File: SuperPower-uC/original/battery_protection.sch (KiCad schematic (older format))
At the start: 11 parts, among them J1 JST_PH_S2B_thru, Q1 DMN2019UTS, U1 AP9101CK6-AYTRG1

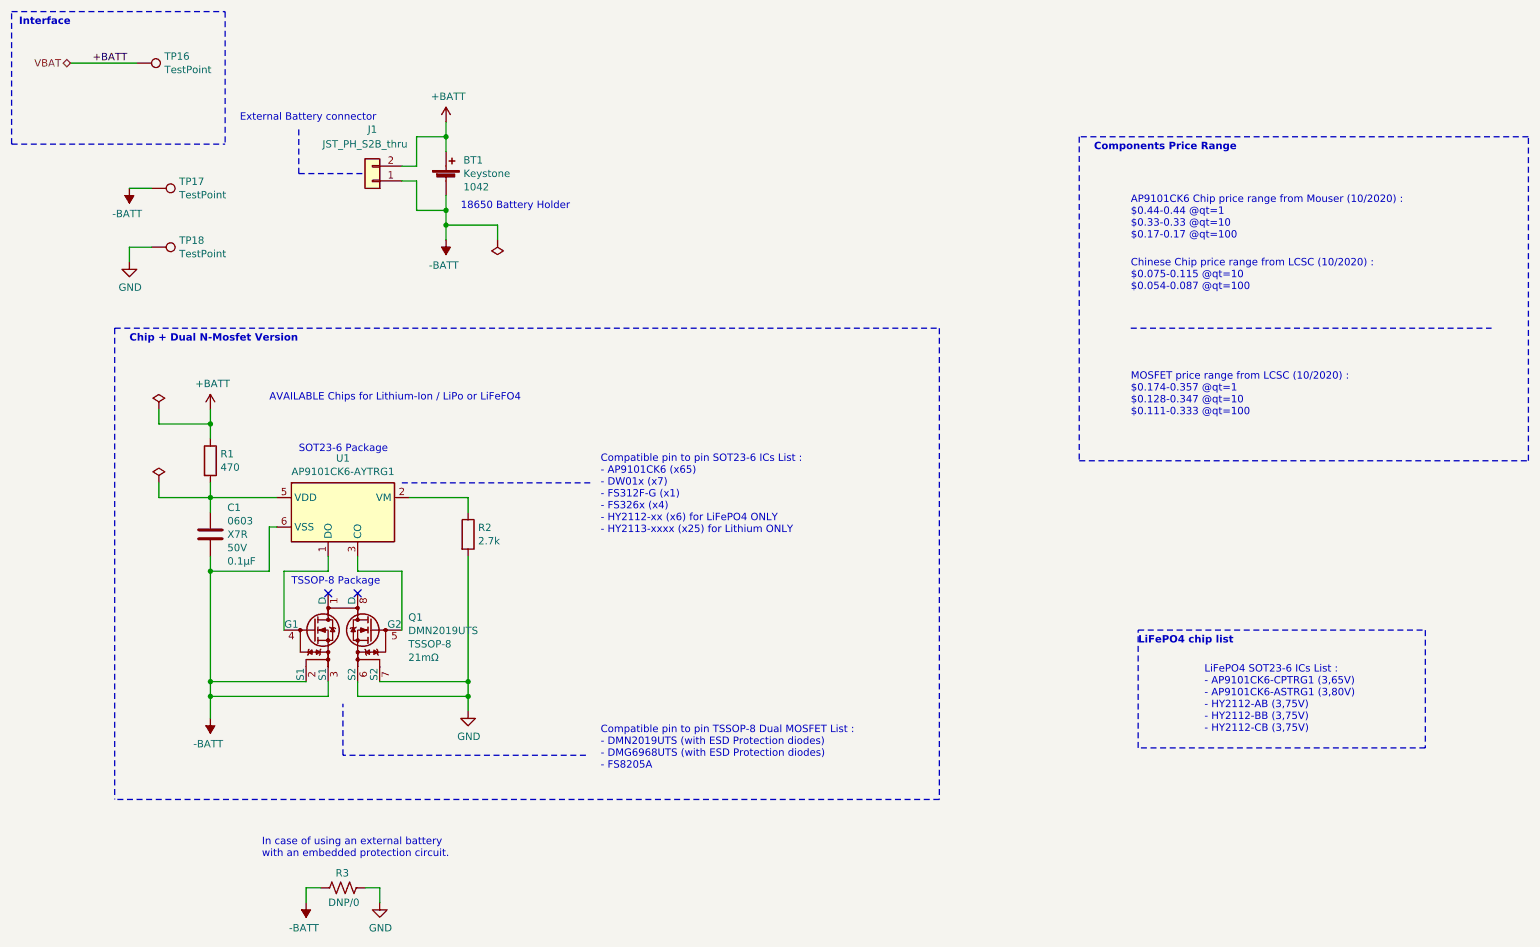
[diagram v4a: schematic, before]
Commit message: Update Battery protection sheet components
+ misc. text
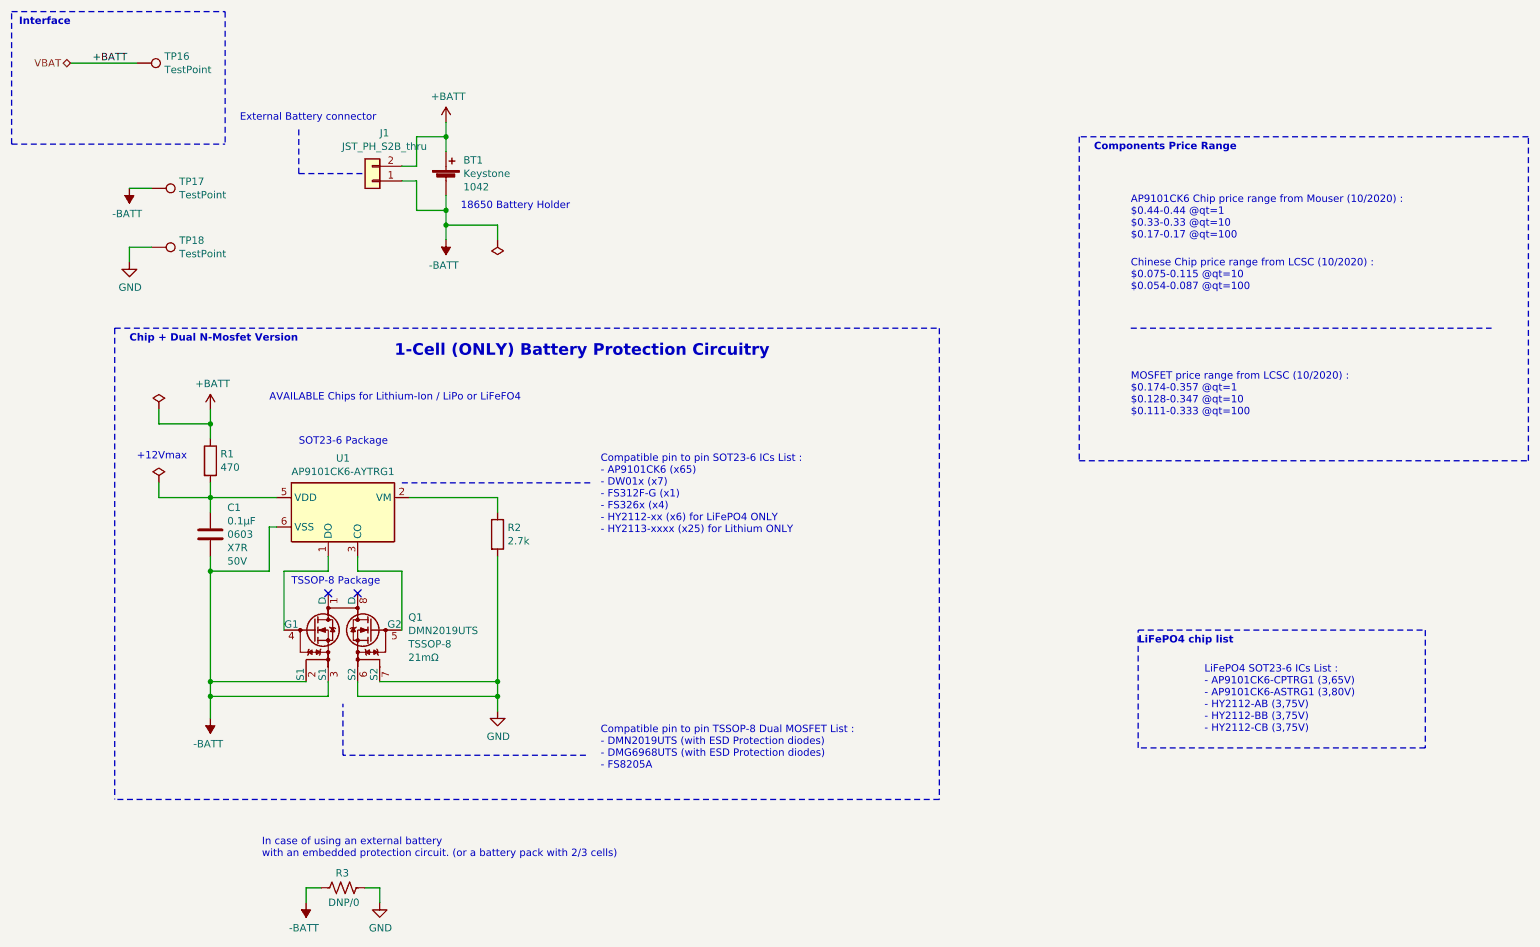
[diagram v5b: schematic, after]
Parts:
- BT1: Farnell_price_qt=100 (none) -> 2,26 €; Farnell_price_qt=1000 (none) -> 1,62 €; Farnell_price_qt=25 2,35 € -> (none); Farnell_price_qt=50 2,30 € -> (none); Farnell_ref (none) -> ?; LCSC_price_qt=1 (none) -> -; LCSC_price_qt=10 (none) -> -; LCSC_price_qt=100 (none) -> -; LCSC_price_qt=1000 (none) -> -; LCSC_ref (none) -> -; LCSC_stock (none) -> -; Mouser_price_qt=10 (none) -> -; Mouser_price_qt=500 $2.61 -> (none); Mouser_ref (none) -> ?; RS_price_qt=1 (none) -> -; RS_price_qt=10 (none) -> -; RS_price_qt=100 (none) -> -; RS_price_qt=1000 (none) -> -; RS_ref (none) -> -; RS_stock (none) -> -; Release_date 2020-11-29 -> 2020-12-12; Release_version 1.00 -> 1.01
- C1: footprint Capacitor_SMD:C_0805_2012Metric -> Capacitor_SMD:C_0603_1608Metric; Farnell_price_qt=1 (none) -> -; Farnell_price_qt=500 0.0221€ -> (none); LCSC_price_qt=1 (none) -> -; LCSC_price_qt=10 (none) -> -; LCSC_price_qt=100 (none) -> $0.0093; LCSC_price_qt=1000 (none) -> $0.0069; LCSC_price_qt=1500 $0.0065 -> (none); LCSC_price_qt=50 $0.0093 -> (none); LCSC_price_qt=500 $0.0069 -> (none); LCSC_price_qt=5000 $0.0061 -> (none); RS_price_qt=1 (none) -> -; RS_price_qt=10 (none) -> -; RS_price_qt=100 (none) -> 0.025€; RS_price_qt=200 0.025€ -> (none); RS_price_qt=2000 0.017€ -> (none); Release_date 2020-11-27 -> 2020-12-12; Release_version 1.00 -> 1.02
- J1: footprint Connector_JST:JST_PH_S2B-PH-K_1x02_P2.00mm_Horizontal -> Connector_JST_user:JST_ZH_S2B-ZR_1x02_P1.50mm_Horizontal; Farnell_price_qt=1 (none) -> -; Farnell_price_qt=10 (none) -> -; LCSC_price_qt=1 (none) -> -; LCSC_price_qt=300 $0.026 -> (none); Mouser_price_qt=1 (none) -> -; Mouser_price_qt=10 (none) -> -; Mouser_price_qt=100 (none) -> -; Mouser_price_qt=1000 (none) -> -; Mouser_stock (none) -> -; RS_price_qt=1 (none) -> -; RS_price_qt=10 (none) -> 0.148€; RS_price_qt=100 (none) -> 0.138€; RS_price_qt=1000 (none) -> 0.068€; RS_price_qt=250 0.088€ -> (none); RS_price_qt=5 0.148€ -> (none); RS_price_qt=50 0.138€ -> (none); RS_price_qt=500 0.068€ -> (none); Release_date 2020-11-24 -> 2020-12-12; Release_version 1.00 -> 1.01
- Q1: Farnell_price_qt=1 (none) -> -; Farnell_price_qt=10 (none) -> -; Farnell_price_qt=1000 (none) -> -; Farnell_price_qt=25 - -> (none); Farnell_price_qt=250 - -> (none); Farnell_price_qt=5 - -> (none); LCSC_price_qt=1000 (none) -> $0.1290; LCSC_price_qt=30 $0.1444 -> (none); Mouser_check_date 2020-12-05 -> 2020-12-13; Mouser_price_qt=1 0,424 € -> $0.505; Mouser_price_qt=10 0,313 € -> $0.372; Mouser_price_qt=100 0,195 € -> $0.232; Mouser_price_qt=1000 (none) -> $0.149; Mouser_price_qt=500 0,181 € -> (none); Mouser_stock 10,295 -> 9,645; Release_date 2020-12-05 -> 2020-12-12; Release_version 1.00 -> 1.01
- U1: Farnell_price_qt=1 (none) -> -; Farnell_price_qt=10 (none) -> -; Farnell_price_qt=100 (none) -> -; Farnell_price_qt=1000 (none) -> -; Farnell_stock (none) -> -; LCSC_check_date 2020-11-22 -> 2020-12-12; LCSC_price_qt=1 $0.503 -> $0.1782; LCSC_price_qt=10 $0.368 -> $0.1304; LCSC_price_qt=100 $0.308 -> $0.1128; LCSC_price_qt=1000 (none) -> $0.107; LCSC_price_qt=30 $0.344 -> (none); LCSC_stock 20 -> 3020; RS_check_date 2020-11-28 -> 2020-12-12; RS_price_qt=1 (none) -> -; RS_price_qt=10 (none) -> -; RS_price_qt=100 (none) -> -; RS_price_qt=1000 (none) -> -; RS_stock (none) -> -; Release_date 2020-11-22 -> 2020-11-23
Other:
- note added: "+12Vmax"
- note added: "1-Cell (ONLY) Battery Protection Circuitry"
- note added: "In case of using an external battery\nwith an embedded protection circuit. (or a battery pack with 2/3 cells)"
- note removed: "In case of using an external battery\nwith an embedded protection circuit."
- moved on the sheet: R2

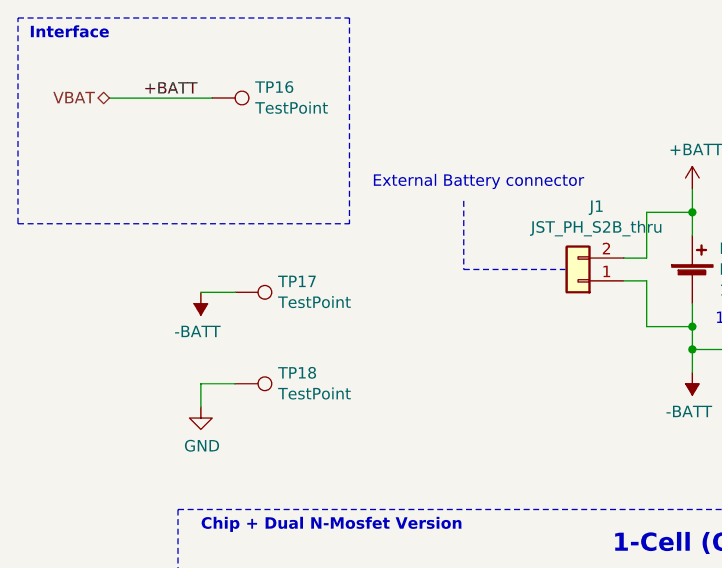
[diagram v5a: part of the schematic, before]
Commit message: Started layout and placed components related to its function and interface (first draft)
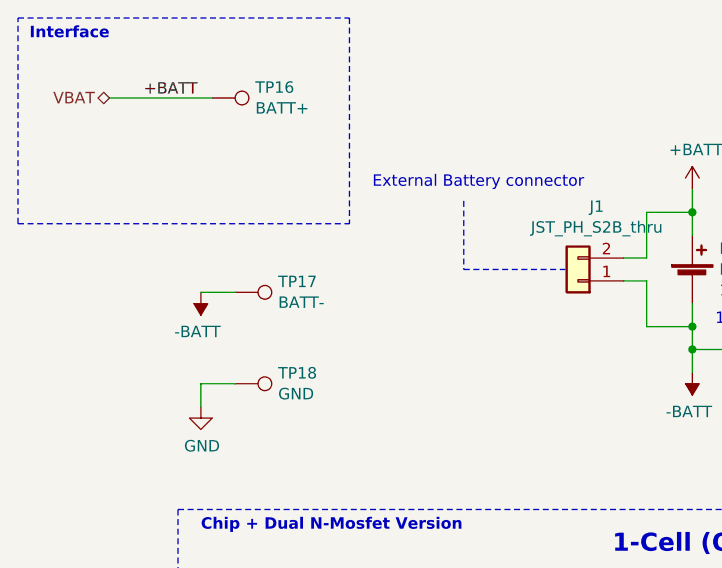
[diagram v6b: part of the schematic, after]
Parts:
- R1: footprint Resistor_SMD:R_0603_1608Metric -> Resistor_SMD:R_0805_2012Metric
- TP16: value TestPoint -> BATT+
- TP17: value TestPoint -> BATT-
- TP18: value TestPoint -> GND
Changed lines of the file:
@@
 F 0 "R1" H 1968 3646 50  0000 L CNN
 F 1 "470" H 1968 3555 50  0000 L CNN
-F 2 "Resistor_SMD:R_0603_1608Metric" V 1940 3590 50  0001 C CNN
+F 2 "Resistor_SMD:R_0805_2012Metric" V 1940 3590 50  0001 C CNN
 F 3 "~" H 1900 3600 50  0001 C CNN
 	1    1900 3600
@@
 P 1400 900
 F 0 "TP16" V 1354 1088 50  0000 L CNN
-F 1 "TestPoint" V 1445 1088 50  0000 L CNN
+F 1 "BATT+" V 1445 1088 50  0000 L CNN
 F 2 "TestPoint:TestPoint_Pad_D1.0mm" H 1600 900 50  0001 C CNN
 F 3 "~" H 1600 900 50  0001 C CNN
@@
 P 1500 1750
 F 0 "TP17" V 1454 1938 50  0000 L CNN
-F 1 "TestPoint" V 1545 1938 50  0000 L CNN
+F 1 "BATT-" V 1545 1938 50  0000 L CNN
 F 2 "TestPoint:TestPoint_Pad_D1.0mm" H 1700 1750 50  0001 C CNN
 F 3 "~" H 1700 1750 50  0001 C CNN
@@
 P 1500 2150
 F 0 "TP18" V 1454 2338 50  0000 L CNN
-F 1 "TestPoint" V 1545 2338 50  0000 L CNN
+F 1 "GND" V 1545 2338 50  0000 L CNN
 F 2 "TestPoint:TestPoint_Pad_D1.0mm" H 1700 2150 50  0001 C CNN
 F 3 "~" H 1700 2150 50  0001 C CNN
